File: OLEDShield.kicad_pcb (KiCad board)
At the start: 2 copper layers, 68.6 x 53.3 mm, 257 parts, among them P1 CONN_5X2, P2 CONN_5X2, P3 CONN_1, P4 CONN_1, P5 CONN_1, SW1 SW_PUSHBUTTON

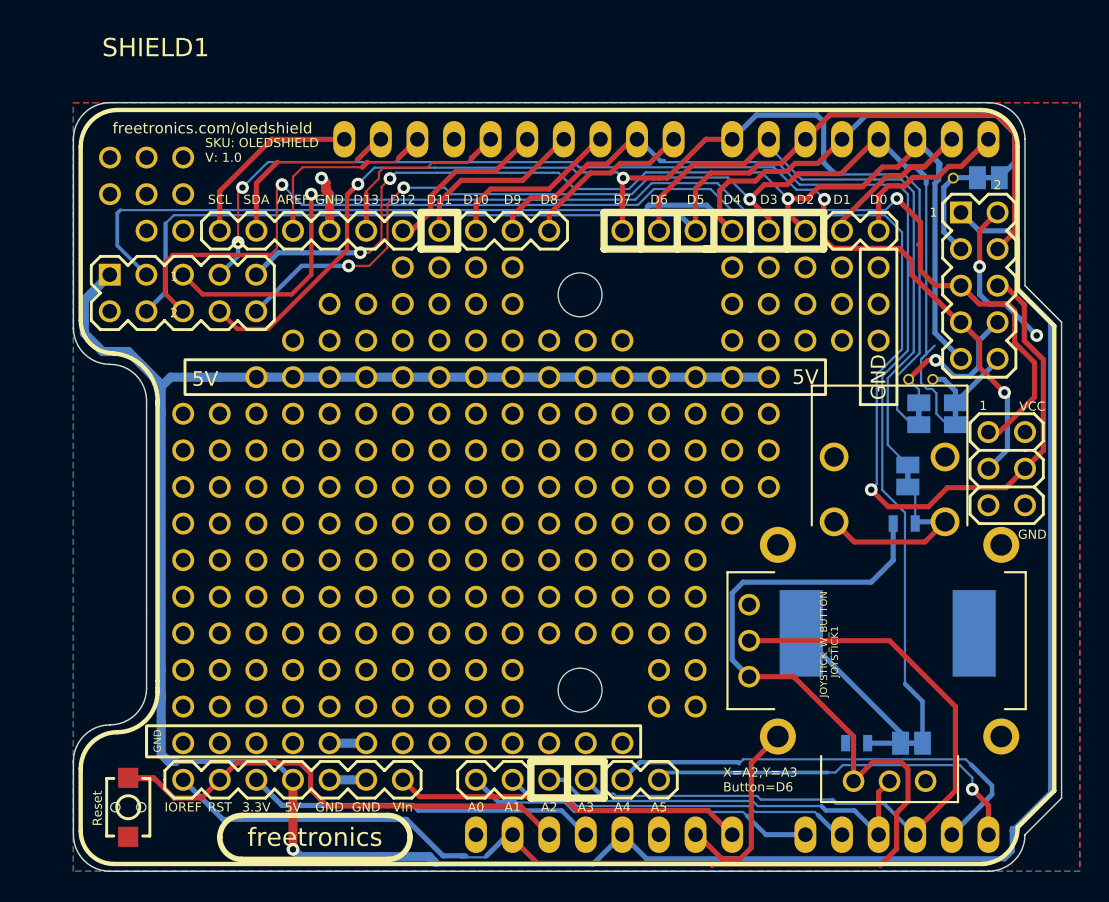
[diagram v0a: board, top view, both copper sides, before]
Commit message: Clean up silkscreen positioning, label formatting
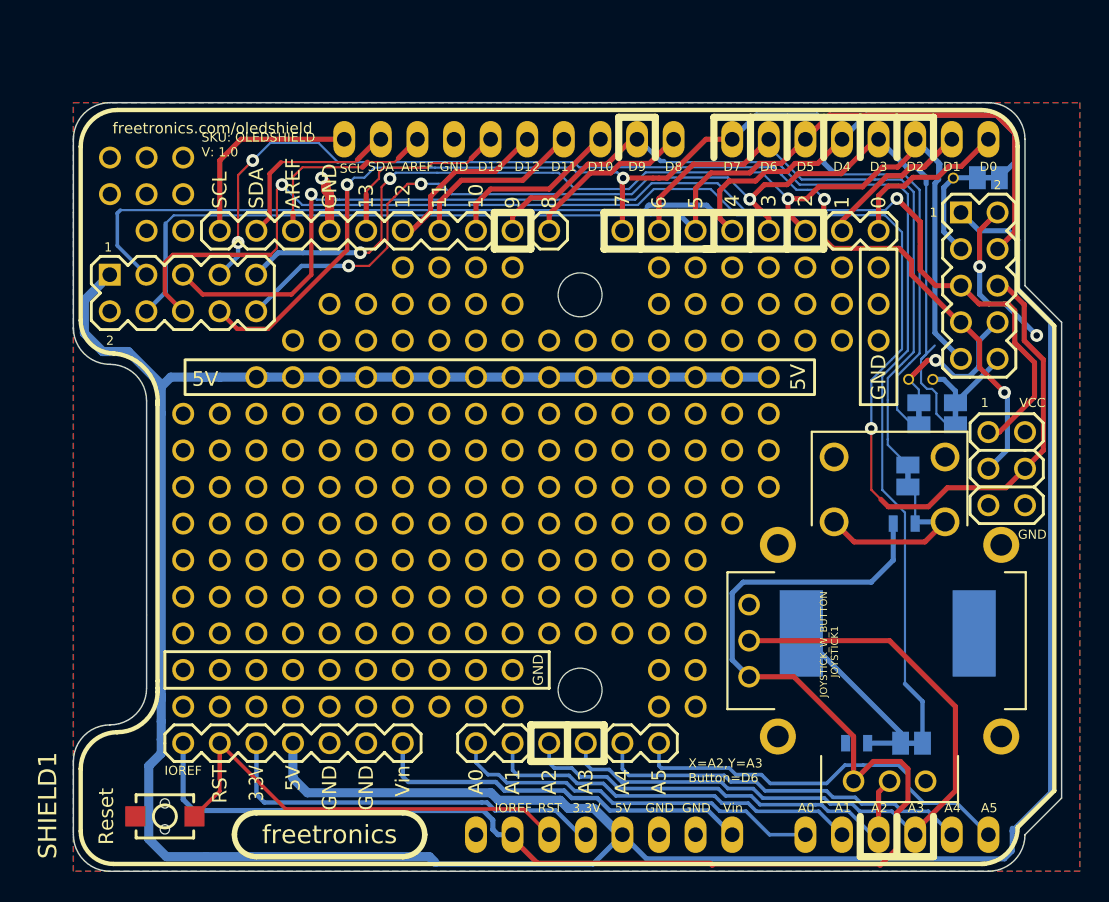
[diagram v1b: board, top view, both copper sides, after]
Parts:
- removed the 1PIN at (256.5, 268.0)
- removed the 1PIN at (254.0, 268.0)
- removed the 1PIN at (251.5, 268.0)
- removed the 1PIN at (238.8, 265.4)
- removed the 1PIN at (241.3, 265.4)
- removed the 1PIN at (243.8, 265.4)
- removed the 1PIN at (246.4, 265.4)
- removed the 1PIN at (248.9, 265.4)
- removed the 1PIN at (226.1, 265.4)
- removed the 1PIN at (228.6, 265.4)
- removed the 1PIN at (231.1, 265.4)
- removed the 1PIN at (233.7, 265.4)
- removed the 1PIN at (236.2, 265.4)
- added 1PIN: P***, 1pin_prototyping, F.Cu at (266.7, 240.0)
- added 1PIN: P***, 1pin_prototyping, F.Cu at (266.7, 237.5)
- added 1PIN: P***, 1pin_prototyping, F.Cu at (266.7, 234.9)
- added 1PIN: P***, 1pin_prototyping, F.Cu at (264.2, 234.9)
- added 1PIN: P***, 1pin_prototyping, F.Cu at (264.2, 237.5)
- added 1PIN: P***, 1pin_prototyping, F.Cu at (264.2, 240.0)
- added Ref**: Val**, LOGO_FREETRONICS_SMALL, B.Cu at (221.9, 271.8)
- moved 1PIN 5.08 mm to (226.1, 262.9)
- moved 1PIN 5.08 mm to (228.6, 262.9)
- moved 1PIN 5.08 mm to (259.1, 240.0)
- moved 1PIN 5.08 mm to (259.1, 237.5)
- moved 1PIN 5.08 mm to (259.1, 234.9)
- moved 1PIN 5.08 mm to (231.1, 262.9)
- moved 1PIN 5.08 mm to (233.7, 262.9)
- moved 1PIN 5.08 mm to (236.2, 262.9)
- moved 1PIN 5.08 mm to (238.8, 262.9)
- moved 1PIN 5.08 mm to (241.3, 262.9)
- moved 1PIN 5.08 mm to (243.8, 262.9)
- moved 1PIN 5.08 mm to (246.4, 262.9)
- moved 1PIN 5.08 mm to (248.9, 262.9)
- moved 1PIN 5.08 mm to (261.6, 234.9)
- moved 1PIN 5.08 mm to (261.6, 237.5)
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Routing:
- net +5V: track 203.1 -> 231.8 mm, vias 1 -> 0
- net GND: track 39.3 -> 20.8 mm
- net /AD4: track 35.6 -> 26.5 mm
- net /RST: track 39.2 -> 33.8 mm
- net /3V3: track 24.4 -> 27.6 mm
- net /MISO: track 83.2 -> 86.4 mm
- net /SCK: track 77.0 -> 80.1 mm
- net /V_IN: track 24.4 -> 26.8 mm
- net /OLED_nRST: track 79.1 -> 81.3 mm
- net VCC: track 99.4 -> 101.5 mm
- net /AD3_JOY_Y: track 50.7 -> 52.6 mm
- net /uSD_CD: track 83.8 -> 82.0 mm
- net /AD2_JOY_X: track 29.2 -> 31.0 mm
- net /AD0: track 27.5 -> 26.3 mm
- net /SCL: track 12.9 -> 14.1 mm
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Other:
- board text added: "0"
- board text added: "10"
- board text added: "11"
- board text added: "12"
- board text added: "13"
- board text added: "3"
- board text added: "4"
- board text added: "5"
- board text added: "6"
- board text added: "7"
- board text added: "8"
- board text added: "9"
- board text added: "Button - D6"
- board text added: "SJ1 Piezo - D9"
- board text added: "Vin"
- board text removed: "Button"
- board text removed: "Piezo"
- board text removed: "SJ1"
- board text removed: "VIn"

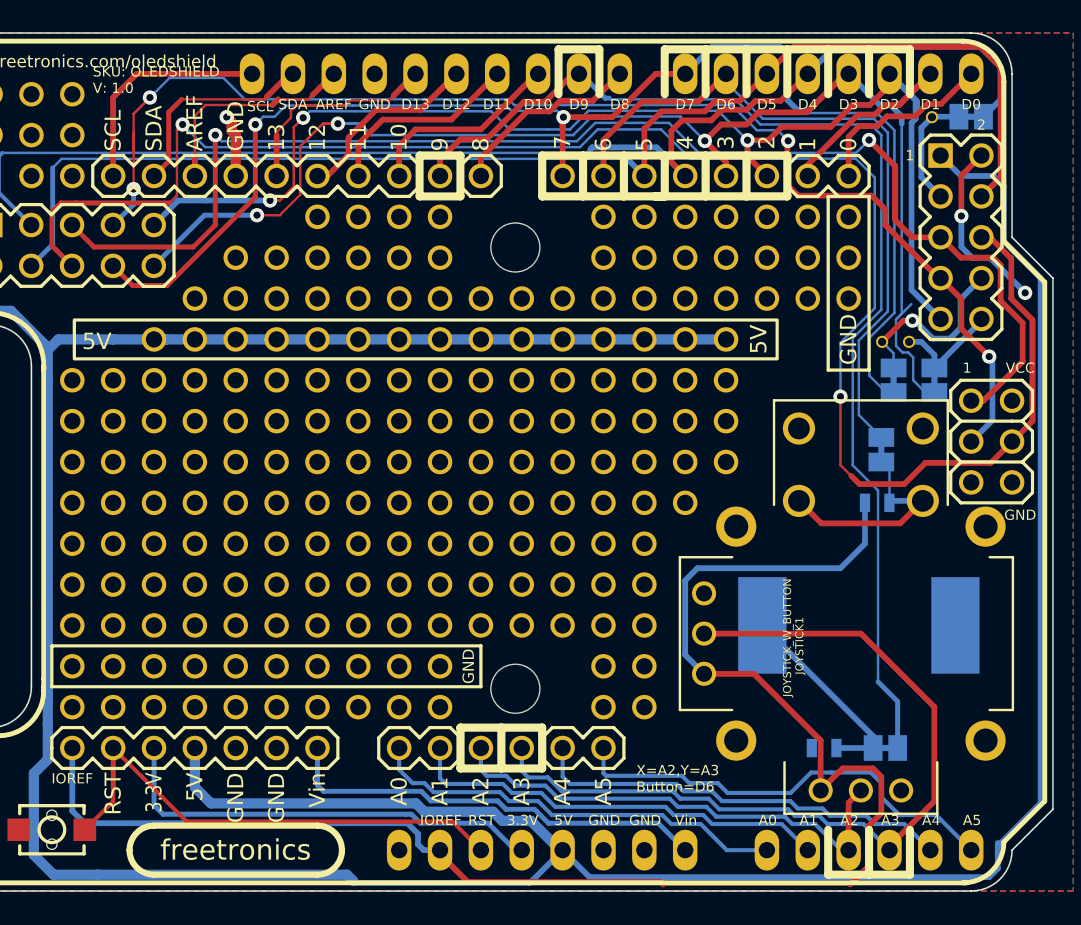
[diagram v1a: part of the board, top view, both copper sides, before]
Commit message: Minor cosmetic/silkscreen cleanups
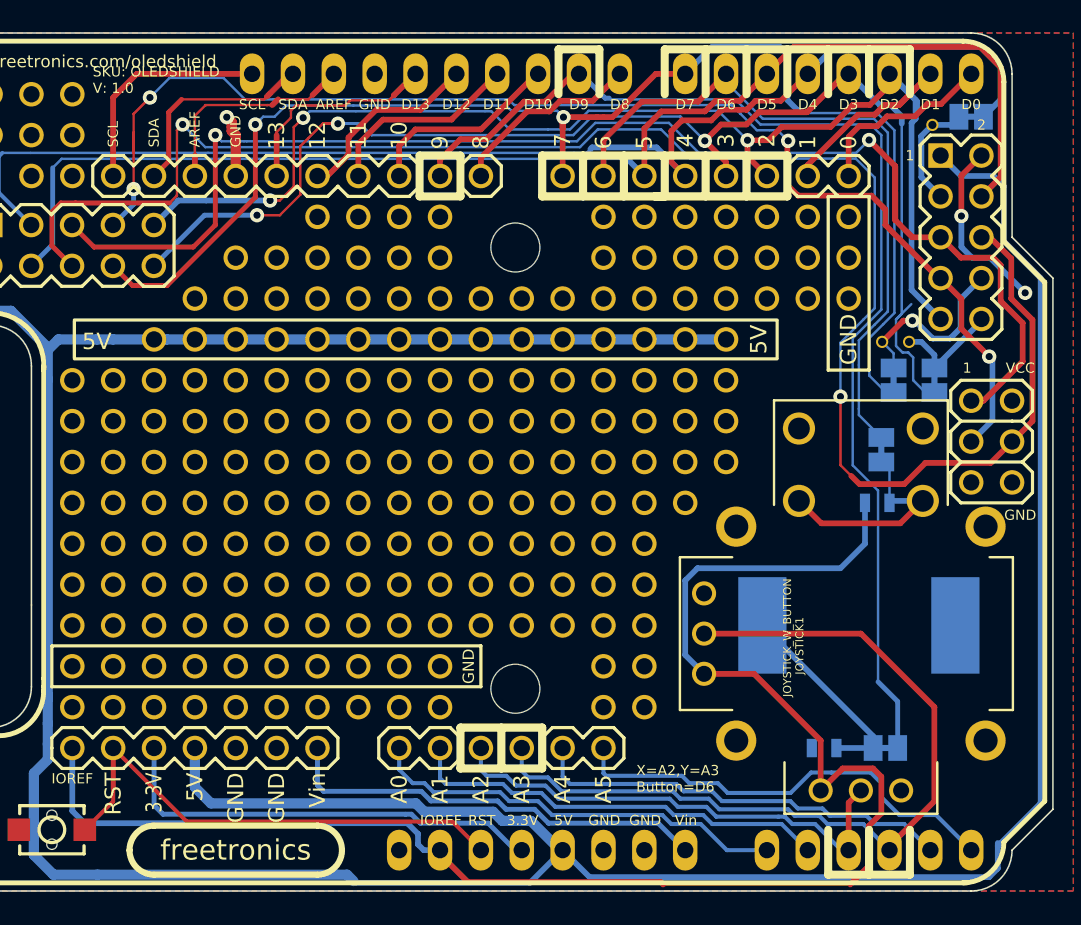
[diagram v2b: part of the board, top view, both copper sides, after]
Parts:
- moved P5 0.48 mm to (279.5, 229.2)
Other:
- board text added: "Button to D6"
- board text added: "Piezo to D9"
- board text added: "SJ1"
- board text removed: "Button - D6"
- board text removed: "SJ1 Piezo - D9"

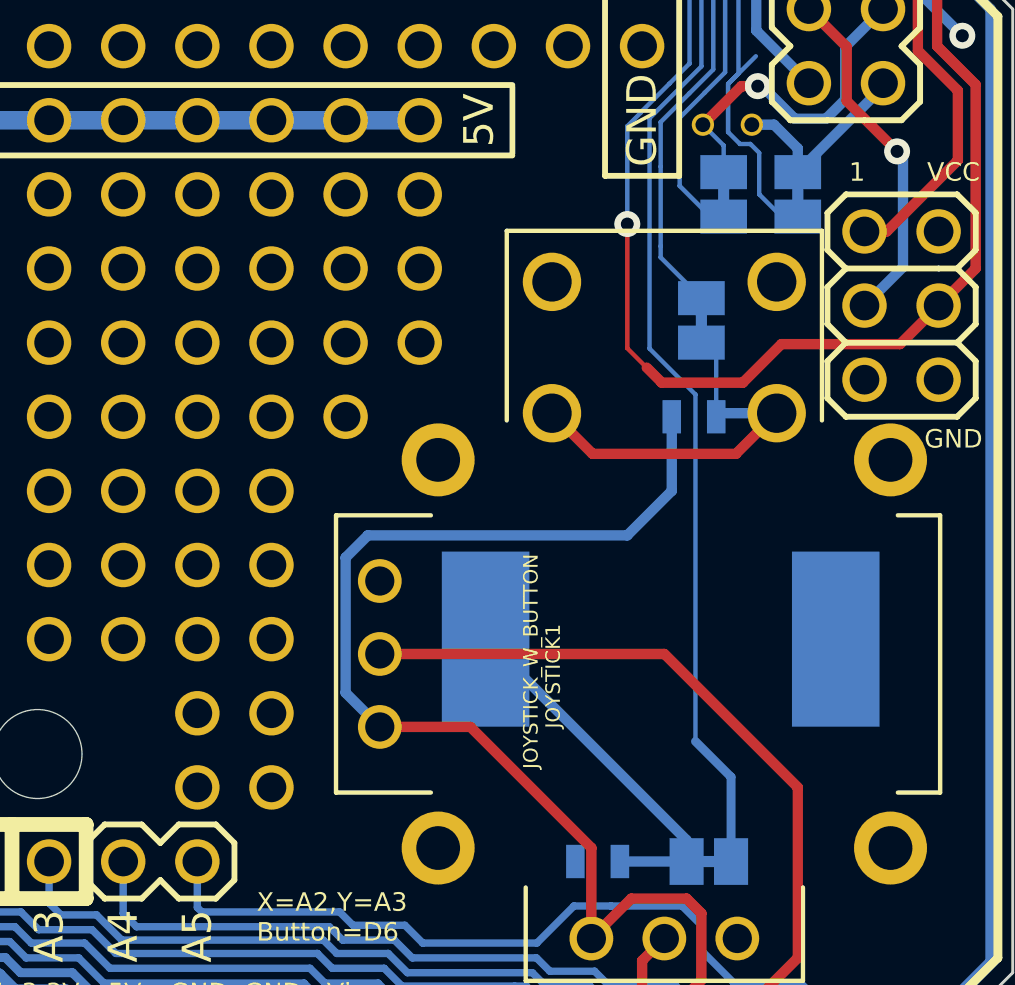
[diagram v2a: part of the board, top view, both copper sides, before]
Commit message: Add pulldown on nRST to hold OLED in reset during board reset
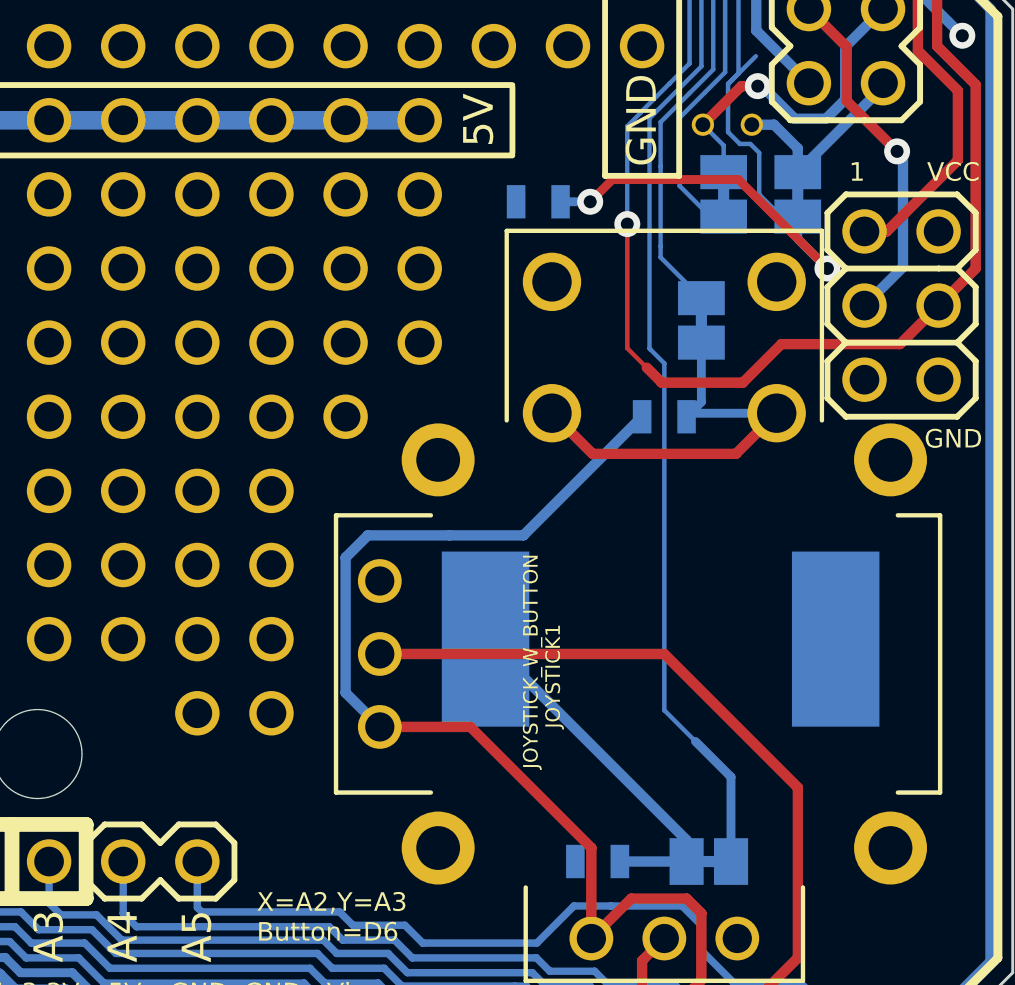
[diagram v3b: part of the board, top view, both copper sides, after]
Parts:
- removed the 1PIN at (261.6, 265.4)
- removed the 1PIN at (259.1, 265.4)
- added R3: 47K, SM0603, B.Cu at (270.8, 245.4)
- moved R2 1.02 mm to (275.1, 252.7)
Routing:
- net /OLED_nRST: track 81.3 -> 94.3 mm, vias 3 -> 5
- net VCC: track 101.5 -> 99.0 mm
- net N-0000025: track 13.7 -> 14.7 mm

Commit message: More minor cosmetic cleanup, bump revision to 1.1
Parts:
- added 1PIN: P***, 1pin_prototyping, F.Cu at (205.7, 129.5)
- added 1PIN: P***, 1pin_prototyping, F.Cu at (208.3, 129.5)
- moved 1PIN 114.8 mm to (238.8, 154.9)
- moved 1PIN 114.8 mm to (236.2, 154.9)
- moved 1PIN 114.8 mm to (233.7, 154.9)
- moved 1PIN 114.8 mm to (231.1, 154.9)
- moved 1PIN 114.8 mm to (228.6, 154.9)
- moved 1PIN 114.8 mm to (226.1, 154.9)
- moved 1PIN 114.8 mm to (221.0, 154.9)
- moved 1PIN 114.8 mm to (218.4, 154.9)
- moved 1PIN 114.8 mm to (215.9, 154.9)
- moved 1PIN 114.8 mm to (213.4, 154.9)
- moved 1PIN 114.8 mm to (210.8, 154.9)
- moved 1PIN 114.8 mm to (208.3, 154.9)
- moved 1PIN 114.8 mm to (205.7, 154.9)
- moved 1PIN 114.8 mm to (238.8, 147.3)
- moved 1PIN 114.8 mm to (241.3, 147.3)
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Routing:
- net GND: track 20.8 -> 27.9 mm, vias 3 -> 4
- net /OLED_nRST: track 94.3 -> 92.9 mm
- net +5V: track 231.8 -> 232.8 mm
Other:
- board text added: "SKU: OLEDSHIELD V: 1.1"
- board text removed: "SKU: OLEDSHIELD V: 1.0"
